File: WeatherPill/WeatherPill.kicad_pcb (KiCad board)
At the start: 2 copper layers, 96.8 x 50.8 mm, 22 parts, among them J2 Conn_02x08_Odd_Even, J3 USB4125-GF-A_REVA2, J4 Conn_02x08_Odd_Even, SW1 EVQ-P7A01P, SW2 EVQ-P7A01P, U1 STM32L052K8Tx, U12 USBLC6-2SC6, U13 BU9796AMUV-E2, U14 SHTC3, U2 SHT40-AD1B-R2, U3 BME280, U4 sst25vf512a-33-4c-sae, U7 STTS22HTR

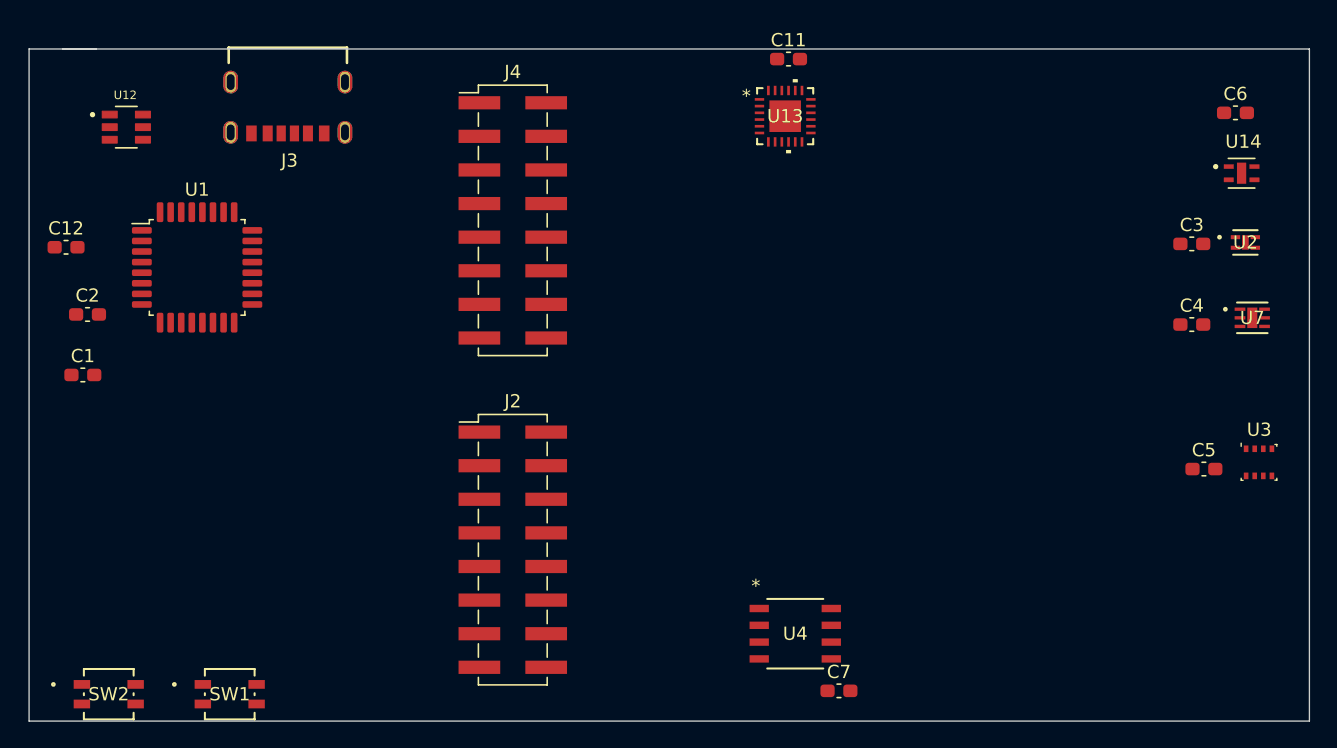
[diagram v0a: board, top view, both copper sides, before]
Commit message: stating to configs pins
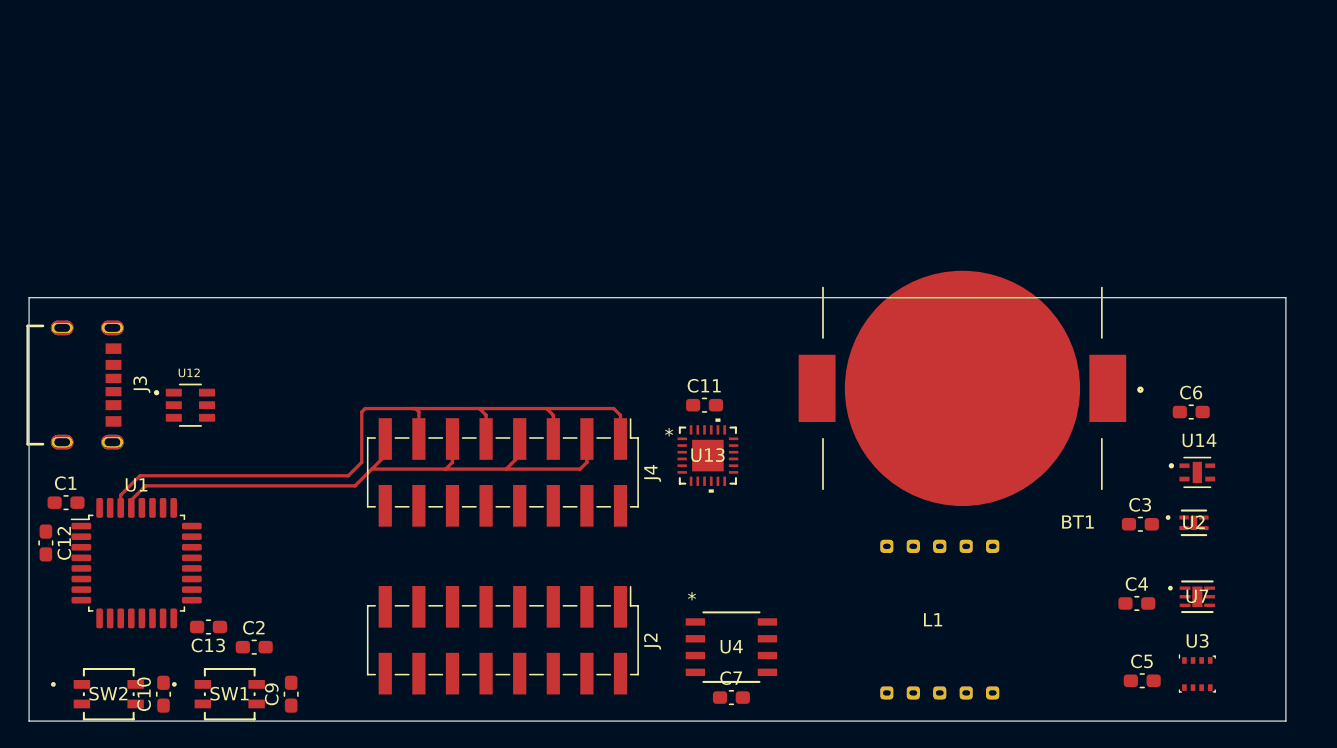
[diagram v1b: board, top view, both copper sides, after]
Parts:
- added BT1: BK-912-TR, BK-912-TR:MPD_BK-912-TR, F.Cu at (98.5, 101.9)
- added C10: 0.1uF, Capacitor_SMD:C_0603_1608Metric_Pad1.08x0.95mm_HandSolder, F.Cu at (38.1, 125.0)
- added C13: 0.1uF, Capacitor_SMD:C_0603_1608Metric_Pad1.08x0.95mm_HandSolder, F.Cu at (41.5, 119.9)
- added C9: 0.1uF, Capacitor_SMD:C_0603_1608Metric_Pad1.08x0.95mm_HandSolder, F.Cu at (47.8, 125.0)
- added L1: ~, Library:lcd_ebay, F.Cu at (94.8, 118.9)
- moved C2 28.1 mm to (45.0, 121.4)
- moved J3 27.4 mm to (31.2, 101.6), turned to -90 degrees
- moved C11 26.9 mm to (79.0, 103.1)
- moved U13 26.3 mm to (79.2, 106.9)
- moved C6 22.9 mm to (115.8, 103.6)
- moved U14 22.9 mm to (116.2, 108.2)
- moved U1 22.8 mm to (36.1, 115.1)
- moved C12 22.4 mm to (29.2, 113.5), turned to -90 degrees
- moved U12 21.6 mm to (40.1, 103.1)
- moved C3 21.5 mm to (111.9, 112.1)
- moved U2 21.5 mm to (116.0, 112.0)
- moved U7 21.5 mm to (116.2, 117.6)
- moved C4 21.5 mm to (111.7, 118.1)
- moved J4 19.1 mm to (63.8, 108.2), turned to -90 degrees
- moved U3 16.7 mm to (116.2, 123.4)
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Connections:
- SW1 pad 1: unconnected-(SW1-Pad1) -> BTN_0
- SW1 pad 1*: unconnected-(SW1-Pad1*) -> V_BUS_3V
- SW1 pad 2: unconnected-(SW1-Pad2) -> GND
- SW1 pad 2*: unconnected-(SW1-Pad2*) -> GND
- SW2 pad 1: unconnected-(SW2-Pad1) -> BTN_1
- SW2 pad 1*: unconnected-(SW2-Pad1*) -> V_BUS_3V
- SW2 pad 2: unconnected-(SW2-Pad2) -> GND
- SW2 pad 2*: unconnected-(SW2-Pad2*) -> GND
- U1 pad 14: unconnected-(U1-PB0-Pad14) -> BTN_0
- U1 pad 15: unconnected-(U1-PB1-Pad15) -> BTN_1
- U1 pad 4: unconnected-(U1-NRST-Pad4) -> NRST
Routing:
- net SDA_1: track 0.00 -> 53.4 mm
- net SCL_1: track 0.00 -> 45.8 mm
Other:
- board size 96.8 x 50.8 mm -> 95 x 32 mm

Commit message: in review
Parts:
- removed C5, C9: 0.1uF, Capacitor_SMD:C_0603_1608Metric_Pad1.08x0.95mm_HandSolder
- removed U12: USBLC6-2SC6, usb tvs:SOT95P280X145-6N
- removed U7: STTS22HTR, STTS22HTR:UDFN-6L_2X2X0P5_STM
- added C8: 100nF, Capacitor_SMD:C_0603_1608Metric_Pad1.08x0.95mm_HandSolder, F.Cu at (63.8, 157.2)
- added H1: MountingHole, MountingHole:MountingHole_3.2mm_M3_DIN965, F.Cu at (76.7, 173.4)
- added H2: MountingHole, MountingHole:MountingHole_3.2mm_M3_DIN965, F.Cu at (121.9, 173.4)
- added H3: MountingHole, MountingHole:MountingHole_3.2mm_M3_DIN965, F.Cu at (122.8, 133.9)
- added H4: MountingHole, MountingHole:MountingHole_3.2mm_M3_DIN965, F.Cu at (52.8, 133.9)
- added J1: Conn_02x05_Odd_Even, Connector_PinSocket_2.54mm:PinSocket_2x05_P2.54mm_Vertical, F.Cu at (52.6, 174.8)
- added J5: Conn_01x02_Pin, Connector_PinHeader_2.54mm:PinHeader_1x02_P2.54mm_Vertical, F.Cu at (78.7, 140.5)
- added Q1: PMOS, Package_TO_SOT_SMD:SOT-323_SC-70_Handsoldering, F.Cu at (75.2, 165.9)
- added Q2: PMOS, Package_TO_SOT_SMD:SOT-323_SC-70_Handsoldering, F.Cu at (70.8, 165.9)
- added Q3: PMOS, Package_TO_SOT_SMD:SOT-323_SC-70_Handsoldering, F.Cu at (66.4, 165.9)
- added R1: 1M, Capacitor_SMD:C_0603_1608Metric_Pad1.08x0.95mm_HandSolder, F.Cu at (62.2, 170.2)
- added R10: 0R, Capacitor_SMD:C_0603_1608Metric_Pad1.08x0.95mm_HandSolder, F.Cu at (59.4, 151.7)
- added R11: 0R, Capacitor_SMD:C_0603_1608Metric_Pad1.08x0.95mm_HandSolder, F.Cu at (111.8, 149.5)
- added R12: 0R, Capacitor_SMD:C_0603_1608Metric_Pad1.08x0.95mm_HandSolder, F.Cu at (122.4, 147.3)
- added R2: 1M, Capacitor_SMD:C_0603_1608Metric_Pad1.08x0.95mm_HandSolder, F.Cu at (70.0, 170.2)
- added R3: 10K, Capacitor_SMD:C_0603_1608Metric_Pad1.08x0.95mm_HandSolder, F.Cu at (83.7, 156.7)
- added R4: 10K, Capacitor_SMD:C_0603_1608Metric_Pad1.08x0.95mm_HandSolder, F.Cu at (83.9, 153.2)
- added R5: 0R, Capacitor_SMD:C_0603_1608Metric_Pad1.08x0.95mm_HandSolder, F.Cu at (107.4, 156.9)
- added R6: 10K, Capacitor_SMD:C_0603_1608Metric_Pad1.08x0.95mm_HandSolder, F.Cu at (90.4, 138.3)
- added R7: 1M, Capacitor_SMD:C_0603_1608Metric_Pad1.08x0.95mm_HandSolder, F.Cu at (73.0, 166.0)
- added R8: 1M, Capacitor_SMD:C_0603_1608Metric_Pad1.08x0.95mm_HandSolder, F.Cu at (68.6, 166.0)
- added R9: 1M, Capacitor_SMD:C_0603_1608Metric_Pad1.08x0.95mm_HandSolder, F.Cu at (64.2, 166.1)
- added SW3: SW_DPDT_x2, dpdt_switch:450404015514, F.Cu at (91.1, 133.4)
- added SW4: SW_DPDT_x2, dpdt_switch:450404015514, F.Cu at (81.0, 133.3)
- added U5: USBLC6-2SC6, Package_TO_SOT_SMD:SOT-23-6, F.Cu at (61.0, 157.2)
- C10, C11, C13, C4, C6: value 0.1uF -> 100nF
- J3: value USB4125-GF-A_REVA2 -> 12402012E212A; footprint usb con:GCT_USB4125-GF-A_REVA2 -> usb conn:12402012E212A_AMP
- moved C12 87.1 mm to (102.6, 160.4), turned to 90 degrees
- moved J4 61.6 mm to (91.7, 163.1), turned to 0 degrees
- moved C11 61.4 mm to (111.8, 155.0), turned to 90 degrees
- moved U13 61.3 mm to (110.7, 159.5)
- moved J3 59.9 mm to (53.9, 157.1)
- moved C13 59.1 mm to (70.0, 171.7), turned to 0 degrees
- moved SW2 57.3 mm to (62.3, 174.8)
- moved SW1 56.5 mm to (69.9, 174.7)
- moved U2 55.6 mm to (101.1, 165.6)
- moved C3 55.6 mm to (76.8, 155.2), turned to 90 degrees
- moved U14 54.4 mm to (100.3, 160.3), turned to -90 degrees
- moved C1 53.9 mm to (65.0, 152.1)
- moved U1 53.8 mm to (70.5, 156.4), turned to 180 degrees
- moved C10 52.6 mm to (62.1, 171.7), turned to 0 degrees
- moved BT1 51.9 mm to (63.3, 140.0), turned to 0 degrees
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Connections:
- net Net-(J2-Pin_10) renamed CS_SST25
- net Net-(J2-Pin_12) renamed SDI_SST25
- net Net-(J2-Pin_14) renamed SDO_SST25
- net Net-(J2-Pin_16) renamed SCK_SST25
- net Net-(J2-Pin_2) renamed CS_BME280
- net Net-(J2-Pin_4) renamed SDI_BME280
- net Net-(J4-Pin_10) renamed SDA_SHT40
- net Net-(J4-Pin_12) renamed SCL_SHT40
- net Net-(J4-Pin_2) renamed SDA_DISPLAY
- net Net-(J4-Pin_4) renamed SCL_DISPLAY
- net Net-(J4-Pin_6) renamed SDA_SHTC3
- net Net-(J4-Pin_8) renamed SCL_SHTC3
- BT1 pad 1: V_BUS_3V -> Net-(J5-Pin_1)
- BT1 pad 2: V_BUS_3V -> Net-(J5-Pin_1)
- C10 pad 2: V_BUS_3V -> Net-(C10-Pad2)
- C11 pad 2: V_BUS_3V -> V_BUS_ZONE_3
- C12 pad 2: V_BUS_3V -> V_BUS_ZONE_2
- C13 pad 2: V_BUS_3V -> Net-(C13-Pad2)
- C4 pad 2: V_BUS_3V -> V_BUS_ZONE_2
- C6 pad 2: V_BUS_3V -> V_BUS_ZONE_2
- C7 pad 2: V_BUS_3V -> V_BUS_ZONE_1
- J2 pad 6: Net-(J2-Pin_6) -> SDO_BME280
- J2 pad 8: Net-(J2-Pin_8) -> SCK_BME280
- J4 pad 14: Net-(J4-Pin_14) -> unconnected-(J4-Pin_14-Pad14)
- J4 pad 16: Net-(J4-Pin_16) -> unconnected-(J4-Pin_16-Pad16)
- L1 pad 1: unconnected-(L1-Pad1) -> Net-(L1-0)
- L1 pad 10: unconnected-(L1-Pad10) -> Net-(L1-A)
- L1 pad 2: unconnected-(L1-Pad2) -> Net-(L1-1)
- L1 pad 3: unconnected-(L1-Pad3) -> Net-(L1-2)
- L1 pad 4: unconnected-(L1-Pad4) -> Net-(L1-3)
- L1 pad 5: unconnected-(L1-Pad5) -> Net-(L1-4)
- L1 pad 6: unconnected-(L1-Pad6) -> Net-(L1-E)
- L1 pad 7: unconnected-(L1-Pad7) -> Net-(L1-D)
- L1 pad 8: unconnected-(L1-Pad8) -> Net-(L1-C)
- L1 pad 9: unconnected-(L1-Pad9) -> Net-(L1-B)
- SW1 pad 1: BTN_0 -> BTN_1
- SW1 pad 1*: V_BUS_3V -> Net-(C13-Pad2)
- SW2 pad 1: BTN_1 -> BTN_2
- SW2 pad 1*: V_BUS_3V -> Net-(C10-Pad2)
- U1 pad 14: BTN_0 -> GND
- U1 pad 15: BTN_1 -> GND
- U1 pad 18: unconnected-(U1-PA8-Pad18) -> BTN_2
- U1 pad 19: unconnected-(U1-PA9-Pad19) -> BTN_1
- U1 pad 2: unconnected-(U1-PC14-Pad2) -> GND
- U1 pad 20: unconnected-(U1-PA10-Pad20) -> GND
- U1 pad 21: unconnected-(U1-PA11-Pad21) -> USB_D-
- U1 pad 22: unconnected-(U1-PA12-Pad22) -> USB_D+
- U1 pad 23: unconnected-(U1-PA13-Pad23) -> SWDIO
- U1 pad 24: unconnected-(U1-PA14-Pad24) -> SWCLK
- U1 pad 25: unconnected-(U1-PA15-Pad25) -> GND
- U1 pad 26: unconnected-(U1-PB3-Pad26) -> CONTROL_ZONE_3
- U1 pad 27: unconnected-(U1-PB4-Pad27) -> CONTROL_ZONE_2
- U1 pad 28: unconnected-(U1-PB5-Pad28) -> CONTROL_ZONE_1
- U1 pad 3: unconnected-(U1-PC15-Pad3) -> GND
- U1 pad 31: unconnected-(U1-BOOT0-Pad31) -> BOOT
- U1 pad 6: unconnected-(U1-PA0-Pad6) -> GND
- U1 pad 7: unconnected-(U1-PA1-Pad7) -> GND
- U1 pad 8: unconnected-(U1-PA2-Pad8) -> GND
- U13 pad 1: unconnected-(U13-OSCIN-Pad1) -> Net-(U13-OSCIN)
- U13 pad 16: unconnected-(U13-COM0-Pad16) -> Net-(L1-A)
- U13 pad 17: unconnected-(U13-COM1-Pad17) -> Net-(L1-B)
- U13 pad 18: unconnected-(U13-COM2-Pad18) -> Net-(L1-C)
- U13 pad 19: unconnected-(U13-COM3-Pad19) -> Net-(L1-D)
- U13 pad 20: unconnected-(U13-VLCD-Pad20) -> GND
- U13 pad 21: V_BUS_3V -> V_BUS_ZONE_3
- U13 pad 4: unconnected-(U13-SEG0-Pad4) -> Net-(L1-0)
- U13 pad 5: unconnected-(U13-SEG1-Pad5) -> Net-(L1-1)
- U13 pad 6: unconnected-(U13-SEG2-Pad6) -> Net-(L1-2)
- U13 pad 7: unconnected-(U13-SEG3-Pad7) -> Net-(L1-3)
- U13 pad 8: unconnected-(U13-SEG4-Pad8) -> Net-(L1-4)
- U13 pad 9: unconnected-(U13-SEG5-Pad9) -> Net-(L1-E)
- U14 pad 1: V_BUS_3V -> V_BUS_ZONE_2
- U2 pad 3: V_BUS_3V -> V_BUS_ZONE_2
- U3 pad 4: Net-(J2-Pin_6) -> SCK_BME280
- U3 pad 5: Net-(J2-Pin_8) -> SDO_BME280
- U3 pad 8: V_BUS_3V -> V_BUS_ZONE_2
- U4 pad 3: unconnected-(U4-*WP-Pad3) -> Net-(U4-*WP)
- U4 pad 7: unconnected-(U4-*HOLD-Pad7) -> Net-(U4-*HOLD)
- U4 pad 8: V_BUS_3V -> V_BUS_ZONE_1
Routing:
- net GND: track 0.00 -> 265.9 mm, vias 0 -> 36
- net V_BUS_ZONE_2: track 0.00 -> 149.5 mm, vias 0 -> 5
- net V_BUS_3V: track 0.00 -> 138.5 mm, vias 0 -> 5
- net V_BUS_ZONE_3: track 0.00 -> 68.9 mm, vias 0 -> 2
- net V_BUS_ZONE_1: track 0.00 -> 66.7 mm, vias 0 -> 2
- net SDO_1: track 0.00 -> 61.8 mm, vias 0 -> 2
- net SDI_1: track 0.00 -> 50.7 mm, vias 0 -> 2
- net SCK_1: track 0.00 -> 46.7 mm
- net CS_1: track 0.00 -> 40.6 mm, vias 0 -> 2
- net Net-(J5-Pin_1): track 0.00 -> 38.8 mm, vias 0 -> 2
- net BOOT: track 0.00 -> 35.7 mm, vias 0 -> 2
- net CS_2: track 0.00 -> 35.2 mm, vias 0 -> 2
- net BTN_2: track 0.00 -> 31.0 mm, vias 0 -> 2
- net BTN_1: track 0.00 -> 29.1 mm, vias 0 -> 2
- net Net-(U5-GND): track 0.00 -> 27.9 mm, vias 0 -> 2
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- added copper zone on B.Cu, net GND
- added copper zone on F.Cu, net GND
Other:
- board size 95 x 32 mm -> 79.8 x 46 mm
- board text added: "CS_1"
- board text added: "CS_2"
- board text added: "SCK_1"
- board text added: "SCL"
- board text added: "SDA"
- board text added: "SDI_1"
- board text added: "SDO_1"

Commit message: roasting
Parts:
- added R13: 0R, Capacitor_SMD:C_0603_1608Metric_Pad1.08x0.95mm_HandSolder, F.Cu at (52.8, 150.7)
- added R14: 0R, Capacitor_SMD:C_0603_1608Metric_Pad1.08x0.95mm_HandSolder, F.Cu at (79.7, 158.5)
- added R15: 0R, Capacitor_SMD:C_0603_1608Metric_Pad1.08x0.95mm_HandSolder, F.Cu at (79.3, 157.0)
- added R16: 0R, Capacitor_SMD:C_0603_1608Metric_Pad1.08x0.95mm_HandSolder, F.Cu at (84.9, 143.1)
- added R17: 0R, Capacitor_SMD:C_0603_1608Metric_Pad1.08x0.95mm_HandSolder, F.Cu at (85.0, 141.5)
- C1, C2, C3: value 0.1uF -> 100nF
- J3: footprint usb conn:12402012E212A_AMP -> usb conn:AMPHENOL_12402012E212A
- R3, R4: value 10K -> 47k
- R6: value 10K -> 1M
- moved R10 1.36 mm to (60.7, 151.3)
- moved J3 1.28 mm to (52.7, 157.1)
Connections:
- J3 pad A5: unconnected-(J3-CC1-PadA5) -> Net-(J3-CC1-PadA5)
- J3 pad B5: unconnected-(J3-CC1-PadB5) -> Net-(J3-CC1-PadB5)
- R11 pad 1: GND -> V_BUS_ZONE_1
- U1 pad 14: GND -> Net-(U1-PB0)
- U1 pad 15: GND -> Net-(U1-PB1)
- U1 pad 2: GND -> Net-(U1-PC14)
- U1 pad 3: GND -> Net-(U1-PC15)
- U14 pad 5: unconnected-(U14-EXP-Pad5) -> GND
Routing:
- net Net-(U1-PB1): track 0.00 -> 22.6 mm
- net Net-(U5-GND): track 27.9 -> 6.01 mm, vias 2 -> 0
- net Net-(U1-PB0): track 0.00 -> 20.8 mm
- net Net-(J3-CC1-PadB5): track 0.00 -> 16.7 mm, vias 0 -> 2
- net GND: track 265.9 -> 253.9 mm, vias 36 -> 48
- net Net-(J3-CC1-PadA5): track 0.00 -> 10.8 mm
- net V_BUS_3V: track 138.5 -> 146.9 mm
- net V_BUS_ZONE_2: track 149.5 -> 155.8 mm
- net Net-(U1-PC14): track 0.00 -> 4.31 mm
- net Net-(U1-PC15): track 0.00 -> 4.22 mm
- net BTN_2: track 31.0 -> 29.1 mm
- net CONTROL_ZONE_1: track 8.28 -> 9.67 mm
- net V_BUS_ZONE_1: track 66.7 -> 67.9 mm, vias 2 -> 3
- net SCK_BME280: track 15.7 -> 15.0 mm
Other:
- board text added: "3V3"
- board text added: "GND"
- board text added: "WeatherPill V1 Frédéric Bilodeau"

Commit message: revision 2
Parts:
- removed C10, C11, C13: 100nF, Capacitor_SMD:C_0603_1608Metric_Pad1.08x0.95mm_HandSolder
- removed C12: 0.1uF, Capacitor_SMD:C_0603_1608Metric_Pad1.08x0.95mm_HandSolder
- removed Q3: PMOS, Package_TO_SOT_SMD:SOT-323_SC-70_Handsoldering
- removed the R1 at (62.2, 170.2)
- removed U13: BU9796AMUV-E2, lcd driver:VQFN024V4040_ROM
- removed U14: SHTC3, SHT3:SON100P200X200X80-5N
- added C5: 100nF, Capacitor_SMD:C_0603_1608Metric_Pad1.08x0.95mm_HandSolder, F.Cu at (27.9, 43.4)
- added C9: 100nF, Capacitor_SMD:C_0603_1608Metric_Pad1.08x0.95mm_HandSolder, F.Cu at (125.1, 83.2)
- added R1: 0R, Capacitor_SMD:C_0603_1608Metric_Pad1.08x0.95mm_HandSolder, F.Cu at (26.6, 53.5)
- added R1: 0R, Capacitor_SMD:C_0603_1608Metric_Pad1.08x0.95mm_HandSolder, F.Cu at (124.0, 118.0)
- added R18: 0R, Capacitor_SMD:C_0603_1608Metric_Pad1.08x0.95mm_HandSolder, F.Cu at (26.5, 50.2)
- added R19: 0R, Capacitor_SMD:C_0603_1608Metric_Pad1.08x0.95mm_HandSolder, F.Cu at (27.0, 63.8)
- added R20: 0R, Capacitor_SMD:C_0603_1608Metric_Pad1.08x0.95mm_HandSolder, F.Cu at (37.0, 66.2)
- BT1: footprint BK-912-TR:MPD_BK-912-TR -> bk-912-tr:MPD_BK-912-TR
- C7: value 0.1uF -> 100nF
- C8: value 100nF -> 0.1uF
- J1: value Conn_02x05_Odd_Even -> Conn_01x02_Pin; footprint Connector_PinSocket_2.54mm:PinSocket_2x05_P2.54mm_Vertical -> Connector_PinHeader_2.54mm:PinHeader_1x02_P2.54mm_Vertical
- J2: value Conn_02x08_Odd_Even -> 12402012E212A; footprint Connector_PinHeader_2.54mm:PinHeader_2x08_P2.54mm_Vertical_SMD -> USB12402012E212A:AMPHENOL_12402012E212A
- J3: value 12402012E212A -> Conn_02x04_Odd_Even; footprint usb conn:AMPHENOL_12402012E212A -> Connector_PinSocket_2.54mm:PinSocket_2x04_P2.54mm_Vertical
- J4: value Conn_02x08_Odd_Even -> Conn_02x05_Odd_Even; footprint Connector_PinHeader_2.54mm:PinHeader_2x08_P2.54mm_Vertical_SMD -> Connector_PinHeader_2.54mm:PinHeader_2x05_P2.54mm_Vertical
- J5: value Conn_01x02_Pin -> Conn_02x08_Odd_Even; footprint Connector_PinHeader_2.54mm:PinHeader_1x02_P2.54mm_Vertical -> Connector_PinHeader_2.54mm:PinHeader_2x08_P2.54mm_Vertical
- R10, R13: value 0R -> 1M
- R11, R12: value 0R -> 47k
- R3, R4: value 47k -> 0R
- R6, R7: value 1M -> 0R
- SW1, SW2: value EVQ-P7A01P -> SW_DPDT_x2; footprint button EVQ:EVQ_P7_PAN -> dpdt_switch:450404015514
- SW3, SW4: value SW_DPDT_x2 -> EVQ-P7A01P; footprint dpdt_switch:450404015514 -> button EVQ:EVQ_P7_PAN
- U1: value STM32L052K8Tx -> USBLC6-2SC6; footprint Package_QFP:LQFP-32_7x7mm_P0.8mm -> Package_TO_SOT_SMD:SOT-23-6
- U2: value SHT40-AD1B-R2 -> STM32L052K8Tx; footprint SHT4x_SEN:SHT4x_SEN -> Package_QFP:LQFP-32_7x7mm_P0.8mm
- U3: value BME280 -> sst25vf512a-33-4c-sae; footprint Package_LGA:Bosch_LGA-8_2.5x2.5mm_P0.65mm_ClockwisePinNumbering -> sst25vf5:SOIC8_SA_SST_MCH
- U4: value sst25vf512a-33-4c-sae -> BU9796AMUV-E2; footprint sst25vf5:SOIC8_SA_SST_MCH -> lcd driver:VQFN024V4040_ROM
- U5: value USBLC6-2SC6 -> BME280; footprint Package_TO_SOT_SMD:SOT-23-6 -> Package_LGA:Bosch_LGA-8_2.5x2.5mm_P0.65mm_ClockwisePinNumbering
- moved SW1 136.8 mm to (93.2, 39.9)
- moved SW2 135.6 mm to (79.5, 40.2)
- moved J1 130.1 mm to (46.0, 44.8)
- moved C4 129.5 mm to (31.5, 58.0), turned to 90 degrees
- moved R8 127.9 mm to (25.9, 45.4), turned to 180 degrees
- moved U2 125.0 mm to (38.7, 57.2), turned to 180 degrees
- moved R7 122.8 mm to (35.8, 49.0)
- moved C6 122.0 mm to (38.2, 43.5), turned to 180 degrees
- moved J2 121.6 mm to (18.1, 58.0), turned to -90 degrees
- moved R5 115.8 mm to (47.2, 58.0), turned to 0 degrees
- moved H1 113.9 mm to (162.5, 98.5)
- moved SW3 112.3 mm to (28.9, 39.9), turned to 180 degrees
- moved C3 112.0 mm to (33.8, 51.9)
- moved U5 109.2 mm to (86.8, 51.0)
- moved C2 108.5 mm to (47.2, 56.2), turned to 0 degrees
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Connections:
- BT1 pad 1: Net-(J5-Pin_1) -> Net-(J1-Pin_1)
- BT1 pad 2: Net-(J5-Pin_1) -> Net-(J1-Pin_1)
- C4 pad 1: GND -> USB_D+
- C4 pad 2: V_BUS_ZONE_2 -> USB_D-
- C6 pad 2: V_BUS_ZONE_2 -> Net-(C6-Pad2)
- C8 pad 1: USB_D+ -> GND
- C8 pad 2: USB_D- -> V_BUS_ZONE_1
- J1 pad 1: POWER_IN -> Net-(J1-Pin_1)
- J1 pad 2: SWDIO -> GND
- J4 pad 10: SDA_SHT40 -> unconnected-(J4-Pin_10-Pad10)
- J4 pad 5: SDA_1 -> V_BUS_ZONE_2
- J4 pad 6: SDA_SHTC3 -> V_BUS_DISPLAY
- J4 pad 7: SCL_1 -> V_BUS_3V
- J4 pad 8: SCL_SHTC3 -> unconnected-(J4-Pin_8-Pad8)
- J4 pad 9: SDA_1 -> GND
- J5 pad 1: Net-(J5-Pin_1) -> CS_1
- J5 pad 2: GND -> CS_BME280
- L1 pad 1: Net-(L1-0) -> Net-(U4-SEG0)
- L1 pad 10: Net-(L1-A) -> Net-(U4-COM0)
- L1 pad 2: Net-(L1-1) -> Net-(U4-SEG1)
- L1 pad 3: Net-(L1-2) -> Net-(U4-SEG2)
- L1 pad 4: Net-(L1-3) -> Net-(U4-SEG3)
- L1 pad 5: Net-(L1-4) -> Net-(U4-SEG4)
- L1 pad 6: Net-(L1-E) -> Net-(U4-SEG5)
- L1 pad 7: Net-(L1-D) -> Net-(U4-COM2)
- L1 pad 8: Net-(L1-C) -> Net-(U4-COM2)
- L1 pad 9: Net-(L1-B) -> Net-(U4-COM0)
- Q1 pad 1: V_BUS_ZONE_1 -> V_BUS_ZONE_2
- Q1 pad 2: CONTROL_ZONE_1 -> CONTROL_ZONE_2
- Q2 pad 1: V_BUS_ZONE_2 -> V_BUS_ZONE_1
- Q2 pad 2: CONTROL_ZONE_2 -> CONTROL_ZONE_1
- R10 pad 1: Net-(U5-GND) -> V_BUS_3V
- R10 pad 2: GND -> CONTROL_ZONE_1
- R11 pad 1: V_BUS_ZONE_1 -> SCL_1
- R11 pad 2: Net-(U4-*WP) -> V_BUS_ZONE_2
- R12 pad 1: Net-(U4-*HOLD) -> SDA_1
- R12 pad 2: GND -> V_BUS_ZONE_2
- R13 pad 1: Net-(J3-CC1-PadA5) -> Net-(C6-Pad2)
- R13 pad 2: Net-(J3-CC1-PadB5) -> V_BUS_3V
- R14 pad 1: Net-(U1-PC14) -> V_BUS_ZONE_1
- R14 pad 2: GND -> Net-(U3-*WP)
- R15 pad 1: Net-(U1-PC15) -> Net-(U4-OSCIN)
- R16 pad 1: Net-(U1-PB0) -> Net-(U3-*HOLD)
- R17 pad 1: Net-(U1-PB1) -> Net-(J2-CC1-PadB5)
- R2 pad 1: Net-(C13-Pad2) -> BOOT
- R2 pad 2: V_BUS_3V -> Net-(SW1A-B)
- R3 pad 1: SCL_1 -> Net-(U1-GND)
- R3 pad 2: V_BUS_3V -> GND
- R4 pad 1: SDA_1 -> Net-(U2-PC14)
- R4 pad 2: V_BUS_3V -> GND
- R5 pad 1: Net-(U13-OSCIN) -> Net-(U2-PC15)
- R6 pad 1: BOOT -> Net-(U2-PB0)
- R6 pad 2: Net-(SW3A-B) -> GND
- R7 pad 1: V_BUS_3V -> Net-(U2-PB1)
- R7 pad 2: CONTROL_ZONE_1 -> GND
- R8 pad 1: V_BUS_3V -> Net-(C5-Pad2)
- R8 pad 2: CONTROL_ZONE_2 -> V_BUS_3V
- R9 pad 2: CONTROL_ZONE_3 -> CONTROL_ZONE_2
- SW1 pad 1: BTN_1 -> V_BUS_3V
- SW2 pad 1: BTN_2 -> V_BUS_3V
- SW3 pad 1: V_BUS_3V -> BTN_1
- SW3 pad 2: Net-(SW3A-B) -> GND
- SW4 pad 1: V_BUS_3V -> BTN_2
- SW4 pad 2: Net-(J5-Pin_1) -> GND
- U1 pad 1: V_BUS_3V -> Net-(J2-D--PadA7)
- U1 pad 2: Net-(U1-PC14) -> Net-(U1-GND)
- U1 pad 3: Net-(U1-PC15) -> Net-(J2-D+-PadA6)
- U1 pad 4: NRST -> USB_D+
- U1 pad 5: V_BUS_3V -> Net-(U1-VBUS)
- U1 pad 6: GND -> USB_D-
- U2 pad 1: SDA_SHT40 -> V_BUS_3V
- U2 pad 2: SCL_SHT40 -> Net-(U2-PC14)
- U2 pad 3: V_BUS_ZONE_2 -> Net-(U2-PC15)
- U2 pad 4: GND -> NRST
- U3 pad 1: GND -> CS_SST25
- U3 pad 2: CS_BME280 -> SDO_SST25
- U3 pad 3: SDI_BME280 -> Net-(U3-*WP)
- U3 pad 4: SCK_BME280 -> GND
- U3 pad 5: SDO_BME280 -> SDI_SST25
- U3 pad 6: unconnected-(U3-VDDIO-Pad6) -> SCK_SST25
- U3 pad 7: GND -> Net-(U3-*HOLD)
- U3 pad 8: V_BUS_ZONE_2 -> V_BUS_ZONE_1
- U4 pad 1: CS_SST25 -> Net-(U4-OSCIN)
- U4 pad 2: SDO_SST25 -> SCL_DISPLAY
- U4 pad 3: Net-(U4-*WP) -> SDA_DISPLAY
- U4 pad 4: GND -> Net-(U4-SEG0)
- U4 pad 5: SDI_SST25 -> Net-(U4-SEG1)
- U4 pad 6: SCK_SST25 -> Net-(U4-SEG2)
- U4 pad 7: Net-(U4-*HOLD) -> Net-(U4-SEG3)
- U4 pad 8: V_BUS_ZONE_1 -> Net-(U4-SEG4)
- U5 pad 1: Net-(J3-D--PadA7) -> GND
- U5 pad 2: Net-(U5-GND) -> CS_BME280
- U5 pad 3: Net-(J3-D+-PadA6) -> SDI_BME280
- U5 pad 4: USB_D+ -> SCK_BME280
- U5 pad 5: Net-(U5-VBUS) -> SDO_BME280
- U5 pad 6: USB_D- -> V_BUS_ZONE_1
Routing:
- net GND: track 253.9 -> 84.7 mm, vias 48 -> 18
- net V_BUS_ZONE_2: track 155.8 -> 12.0 mm, vias 5 -> 1
- net V_BUS_3V: track 146.9 -> 9.53 mm, vias 5 -> 0
- net V_BUS_ZONE_3: track 68.9 -> 0.00 mm, vias 2 -> 0
- net V_BUS_ZONE_1: track 67.9 -> 4.05 mm, vias 3 -> 0
- net Net-(J5-Pin_1): track 38.8 -> 0.00 mm, vias 2 -> 0
- net BOOT: track 36.2 -> 0.00 mm, vias 2 -> 0
- net SDA_1: track 51.3 -> 17.5 mm, vias 2 -> 0
- net SCL_1: track 49.2 -> 16.2 mm
- net NRST: track 26.9 -> 0.00 mm, vias 2 -> 0
- net Net-(U1-PB1): track 22.6 -> 0.00 mm
- net SDO_1: track 61.8 -> 39.3 mm, vias 2 -> 0
- net Net-(U1-PB0): track 20.8 -> 0.00 mm
- net SDI_BME280: track 9.95 -> 29.5 mm
- net Net-(L1-E): track 19.0 -> 0.00 mm
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- removed copper zone on F.Cu, net GND
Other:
- board size 79.8 x 46 mm -> 319.5 x 201 mm
- board text removed: "3V3"
- board text removed: "CS_1"
- board text removed: "CS_2"
- board text removed: "GND"
- board text removed: "SCK_1"
- board text removed: "SCL"
- board text removed: "SDA"
- board text removed: "SDI_1"
- board text removed: "SDO_1"
- board text removed: "WeatherPill V1 Frédéric Bilodeau"
